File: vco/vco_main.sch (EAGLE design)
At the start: 82 parts, among them IC1 OPA4130U, IC2 LM13700M, IC3 OPA4130U, IC4 OPA4130U, Q1 MMBFJ3

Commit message: added gerbers
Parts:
- added C10, C11, C12, C13, C14, C15, C16, C17, C18, C19, C8, C9: 1n, dan:C-USC0603
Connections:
- net +12V: now also C14.1, C15.1, C16.1, C17.1, C18.1, C19.1, IC2G$5.V+, POWER-10.KL, POWER-9.KL
- net -12V: now also C10.1, C11.1, C12.1, C13.1, C8.1, C9.1, IC2G$5.V-, POWER-1.KL, POWER-2.KL
- net GND: now also C10.2, C11.2, C12.2, C13.2, C14.2, C15.2, C16.2, C17.2, C18.2, C19.2, C8.2, C9.2, POWER-3.KL, POWER-4.KL, POWER-5.KL, POWER-6.KL, POWER-7.KL, POWER-8.KL

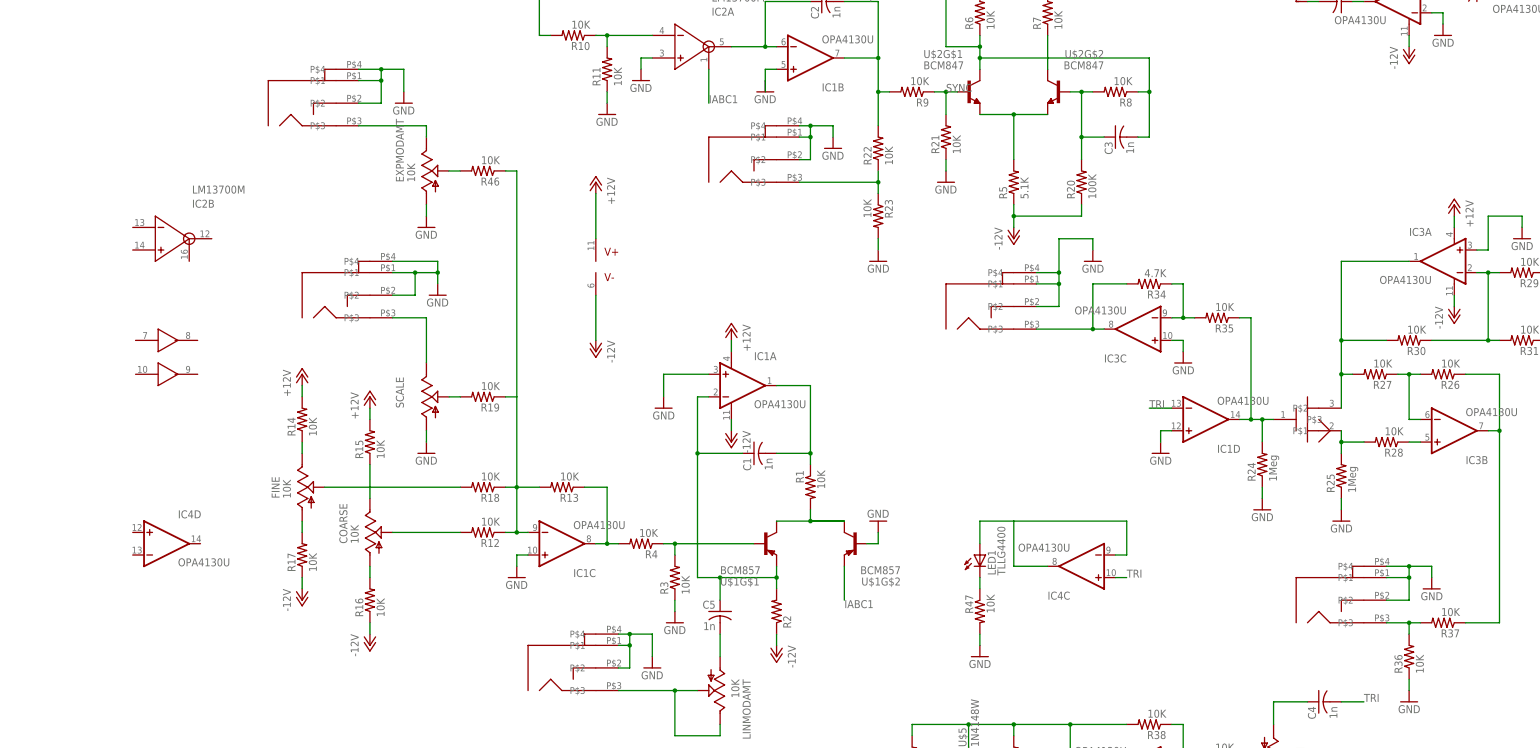
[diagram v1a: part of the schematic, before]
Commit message: fixed the schematic.  need to check polarity on current source and square comparator.  moved most of the labels to the silkscreen layer, but need to do that with the new components.
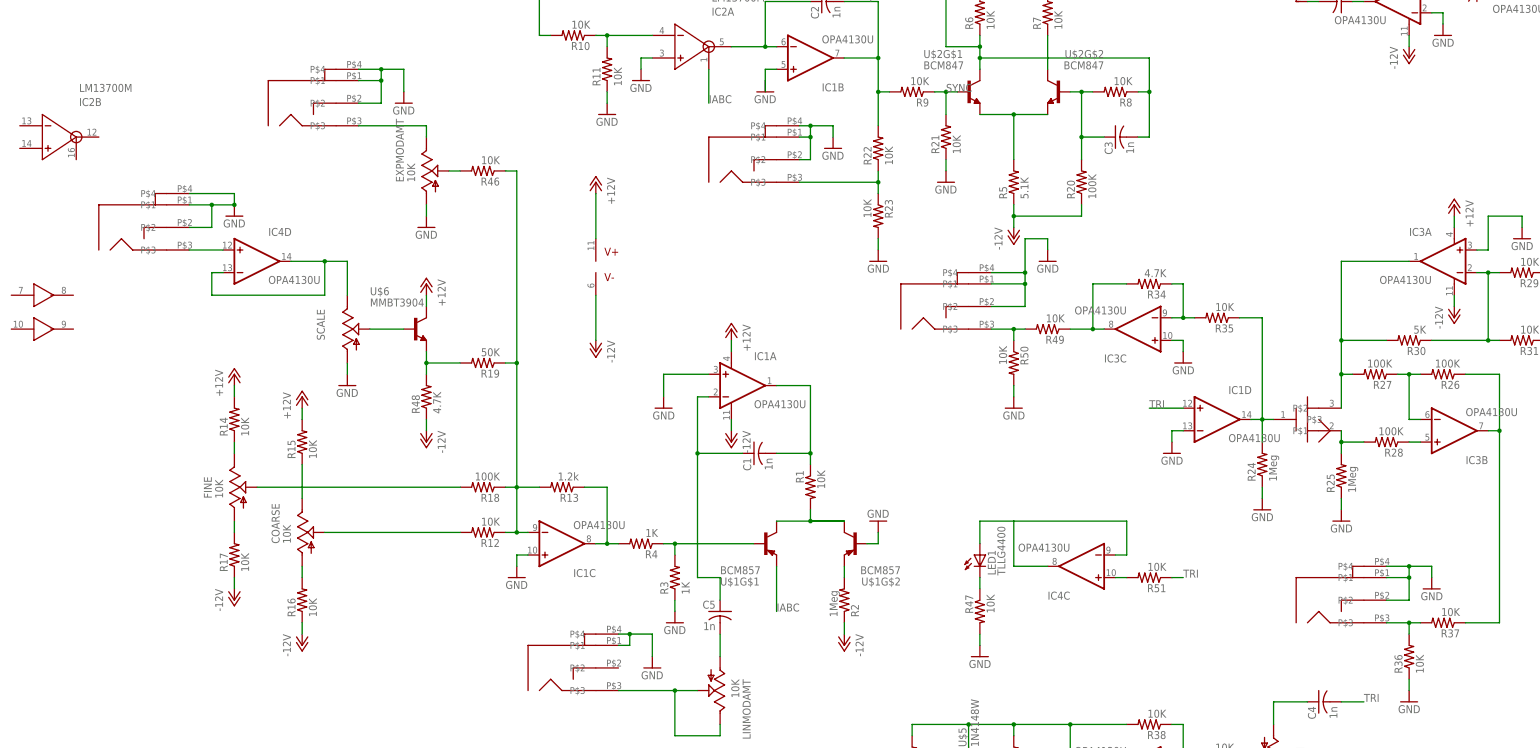
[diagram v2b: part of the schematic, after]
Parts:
- added R48: 4.7K, dan:R-US_R0603
- added R49, R50, R51: 10K, dan:R-US_R0603
- added U$6: MMBT3904, dan:MMBT3904
- R13: value 10K -> 1.2k
- R18, R26, R27, R28: value 10K -> 100K
- R19: value 10K -> 50K
- R2: value (none) -> 1Meg
- R3, R4: value 10K -> 1K
- R30: value 10K -> 5K
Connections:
- removed net IABC1: IC2A.IABC, U$1G$2.E
- new net IABC: IC2A.IABC, U$1G$1.E
- new net N$54: IC4D.+IN, VPEROCT.P$3
- new net N$55: IC4D.-IN, IC4D.OUT, SCALE.E
- new net N$56: SCALE.S, U$6.B
- new net N$58: R51.1
- new net N$9: R49.2, R50.1, SQUARE.P$3
- net +12V: now also U$6.C
- net -12V: now also R48.1
- net GND: now also IC1D.-IN, R50.2; no longer IC1D.+IN, LINMOD.P$2
- net N$22: now also R48.2, U$6.E; no longer SCALE.S
- net N$24: now also R2.2, U$1G$2.E; no longer SCALE.E, VPEROCT.P$3
- net N$3: no longer R2.2, U$1G$1.E
- net N$36: now also R49.1; no longer SQUARE.P$3
- net TRI: now also IC1D.+IN, R51.2; no longer IC1D.-IN
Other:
- moved on the sheet: COARSE, FINE, IC1D, IC2B, IC4D, R14, R15, R16, R17, R19, R2, SCALE

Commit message: fixed schematic.  moved all labels to silkscreen.  fixed layout.  need to make gerbers.
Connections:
- removed net N$58: R51.1
- new net N$59: IC4C.+IN, R51.2
- net TRI: now also R51.1; no longer IC4C.+IN, R51.2
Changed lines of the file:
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@@
-</segment>
-<segment>
-<pinref part="IC4" gate="C" pin="+IN"/>
-<wire x1="149.86" y1="7.62" x2="152.4" y2="7.62" width="0.1524" layer="91"/>
-<label x="165.1" y="7.62" size="1.778" layer="95"/>
-<pinref part="R51" gate="G$1" pin="2"/>
 </segment>
 <segment>
@@
 <wire x1="165.1" y1="45.72" x2="157.48" y2="45.72" width="0.1524" layer="91"/>
 <label x="157.48" y="45.72" size="1.778" layer="95"/>
+</segment>
+<segment>
+<pinref part="R51" gate="G$1" pin="1"/>
+<wire x1="165.1" y1="7.62" x2="162.56" y2="7.62" width="0.1524" layer="91"/>
+<label x="165.1" y="7.62" size="1.778" layer="95"/>
 </segment>
 </net>
@@
 </segment>
 </net>
-<net name="N$58" class="0">
-<segment>
-<pinref part="R51" gate="G$1" pin="1"/>
-<wire x1="165.1" y1="7.62" x2="162.56" y2="7.62" width="0.1524" layer="91"/>
-</segment>
-</net>
+<net name="N$59" class="0">
+<segment>
+<pinref part="IC4" gate="C" pin="+IN"/>
+<pinref part="R51" gate="G$1" pin="2"/>
+<wire x1="149.86" y1="7.62" x2="152.4" y2="7.62" width="0.1524" layer="91"/>
+</segment>
+</net>

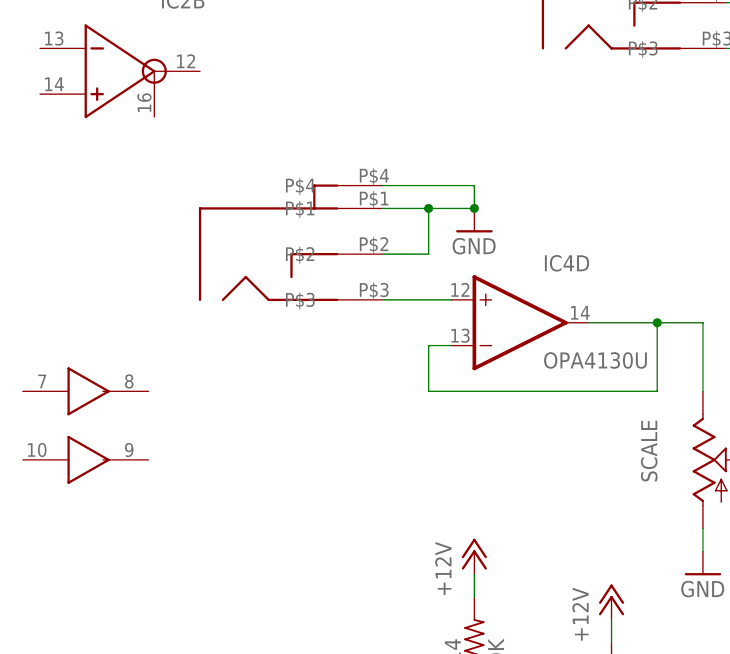
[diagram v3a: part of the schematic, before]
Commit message: fixed some drc errors.  made gerbers.  silkscreen gerber doesn't seem to be getting the fonts correctly.
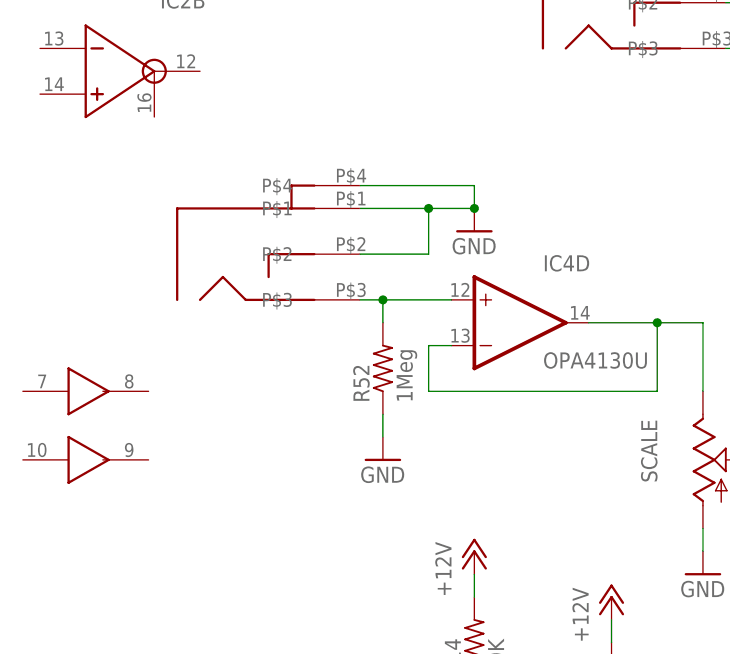
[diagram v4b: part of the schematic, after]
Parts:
- added R52: 1Meg, dan:R-US_R0603
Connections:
- net GND: now also R52.1
- net N$54: now also R52.2
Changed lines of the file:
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@@
 <part name="GND36" library="dan" deviceset="GND" device=""/>
 <part name="R51" library="dan" deviceset="R-US_" device="R0603" value="10K"/>
+<part name="R52" library="dan" deviceset="R-US_" device="R0603" value="1Meg"/>
+<part name="GND37" library="dan" deviceset="GND" device=""/>
 </parts>
 <sheets>
@@
 <instance part="GND8" gate="1" x="-22.86" y="50.8"/>
 <instance part="GND9" gate="1" x="-48.26" y="88.9"/>
-<instance part="VPEROCT" gate="G$1" x="-68.58" y="86.36"/>
+<instance part="VPEROCT" gate="G$1" x="-71.12" y="86.36"/>
 <instance part="GND7" gate="1" x="71.12" y="116.84"/>
 <instance part="C2" gate="G$1" x="83.82" y="137.16" rot="MR270"/>
@@
 <instance part="GND36" gate="1" x="127" y="45.72" rot="MR0"/>
 <instance part="R51" gate="G$1" x="157.48" y="7.62" rot="R180"/>
+<instance part="R52" gate="G$1" x="-58.42" y="73.66" rot="R90"/>
+<instance part="GND37" gate="1" x="-58.42" y="63.5"/>
 </instances>
 <busses>
@@
 <pinref part="VPEROCT" gate="G$1" pin="P$4"/>
 <wire x1="-48.26" y1="91.44" x2="-48.26" y2="93.98" width="0.1524" layer="91"/>
-<wire x1="-48.26" y1="93.98" x2="-58.42" y2="93.98" width="0.1524" layer="91"/>
+<wire x1="-48.26" y1="93.98" x2="-60.96" y2="93.98" width="0.1524" layer="91"/>
 <pinref part="VPEROCT" gate="G$1" pin="P$1"/>
-<wire x1="-58.42" y1="91.44" x2="-53.34" y2="91.44" width="0.1524" layer="91"/>
+<wire x1="-60.96" y1="91.44" x2="-53.34" y2="91.44" width="0.1524" layer="91"/>
 <pinref part="VPEROCT" gate="G$1" pin="P$2"/>
 <wire x1="-53.34" y1="91.44" x2="-48.26" y2="91.44" width="0.1524" layer="91"/>
-<wire x1="-58.42" y1="86.36" x2="-53.34" y2="86.36" width="0.1524" layer="91"/>
+<wire x1="-60.96" y1="86.36" x2="-53.34" y2="86.36" width="0.1524" layer="91"/>
 <wire x1="-53.34" y1="86.36" x2="-53.34" y2="91.44" width="0.1524" layer="91"/>
 <junction x="-53.34" y="91.44"/>
@@
 <wire x1="127" y1="48.26" x2="127" y2="50.8" width="0.1524" layer="91"/>
 </segment>
+<segment>
+<pinref part="GND37" gate="1" pin="GND"/>
+<pinref part="R52" gate="G$1" pin="1"/>
+<wire x1="-58.42" y1="66.04" x2="-58.42" y2="68.58" width="0.1524" layer="91"/>
+</segment>
 </net>
 <net name="N$7" class="0">
@@
 <pinref part="VPEROCT" gate="G$1" pin="P$3"/>
 <wire x1="-50.8" y1="81.28" x2="-58.42" y2="81.28" width="0.1524" layer="91"/>
-</segment>
-</net>
+<pinref part="R52" gate="G$1" pin="2"/>
+<wire x1="-58.42" y1="81.28" x2="-60.96" y2="81.28" width="0.1524" layer="91"/>
+<wire x1="-58.42" y1="78.74" x2="-58.42" y2="81.28" width="0.1524" layer="91"/>
+<junction x="-58.42" y="81.28"/>
+</segment>
+</net>

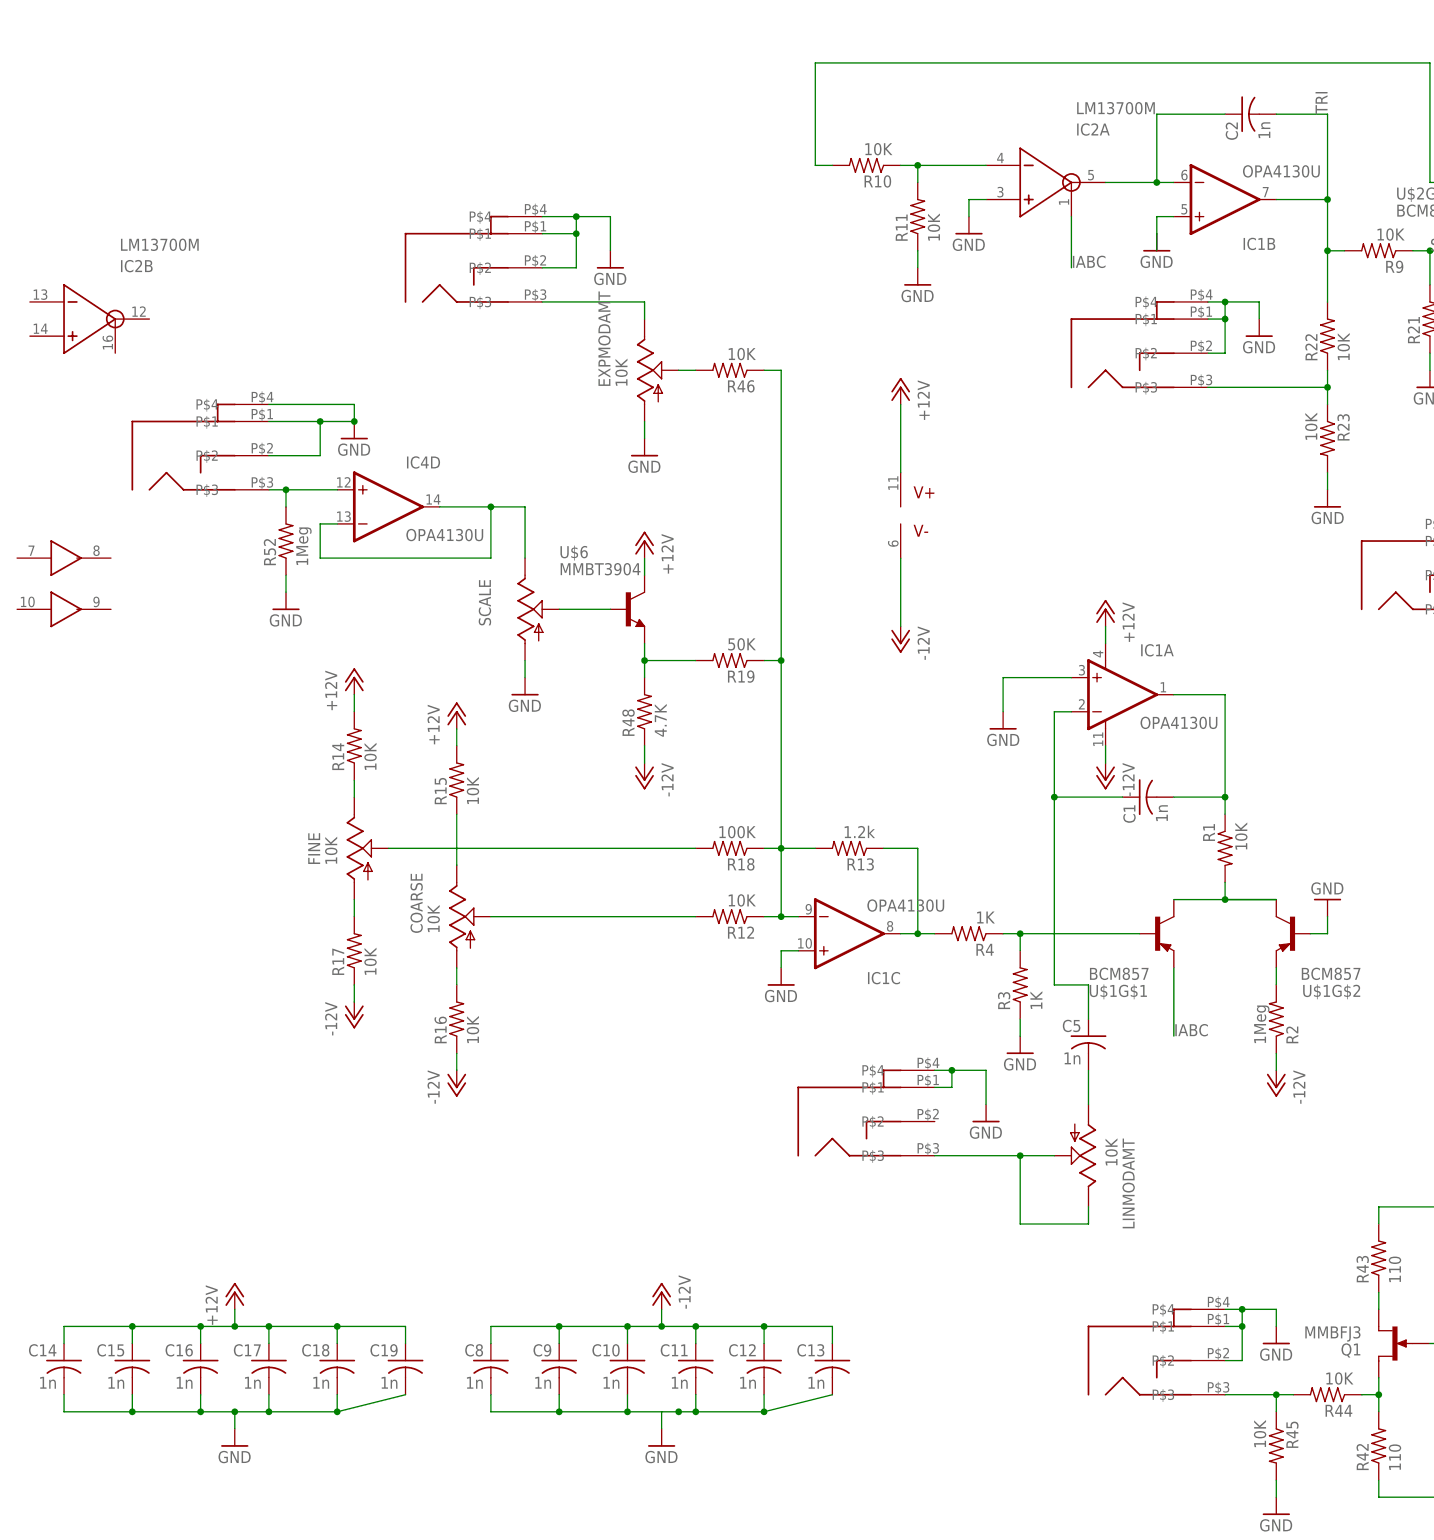
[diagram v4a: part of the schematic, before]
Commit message: fixed silkscreen.  fixed linear mod.  started to think about critical nets.
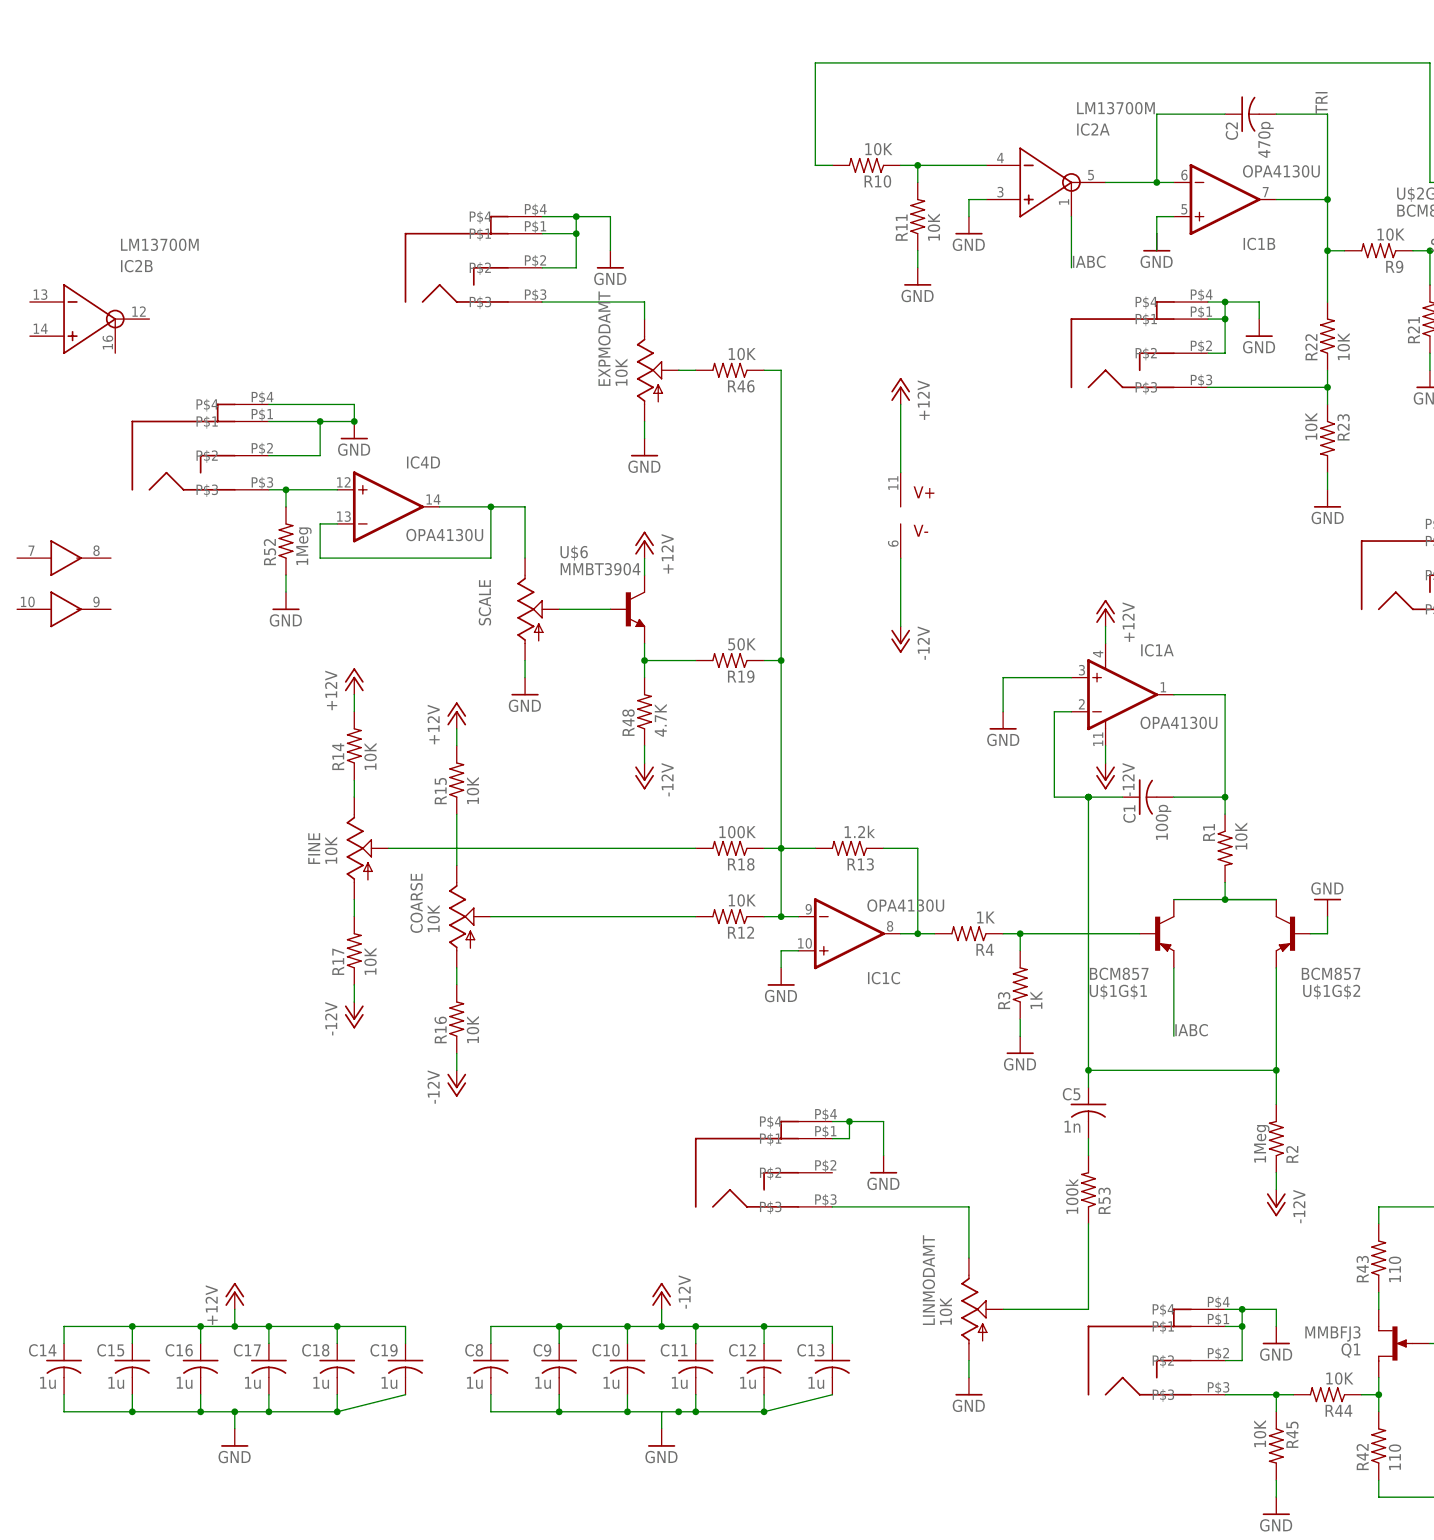
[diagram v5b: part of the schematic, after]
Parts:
- added R53: 100k, dan:R-US_R0603
- C1: value 1n -> 100p
- C10, C11, C12, C13, C14, C15, C16, C17, C18, C19, C8, C9: value 1n -> 1u
- C2: value 1n -> 470p
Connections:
- net GND: now also LINMODAMT.A
- net N$24: now also LINMOD.P$3, LINMODAMT.E; no longer R2.2, U$1G$2.E
- net N$3: now also R2.2, U$1G$2.E
- net N$46: now also R53.1; no longer LINMOD.P$3, LINMODAMT.E
- net N$48: now also R53.2; no longer LINMODAMT.A
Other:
- moved on the sheet: C5, LINMODAMT, R2
